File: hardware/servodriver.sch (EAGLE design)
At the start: 17 parts, among them IC1 PIC12F683P, IC2 7805

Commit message: Add the CAM files
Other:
- note added: "2"
- note added: "ServoDriver for the Stockton Marine Science Program. MIT License. (c) 2014 Chris Luke. Source code at https://github.com/chrisy/pic12servo"
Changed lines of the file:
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@@
 <sheet>
 <plain>
+<text x="150.114" y="24.384" size="1.778" layer="91">ServoDriver for the Stockton Marine Science Program.
+MIT License. (c) 2014 Chris Luke.
+Source code at https://github.com/chrisy/pic12servo</text>
+<text x="241.3" y="7.62" size="1.778" layer="91">2</text>
 </plain>
 <instances>
@@
 </schematic>
 </drawing>
+<compatibility>
+<note version="6.3" minversion="6.2.2" severity="warning">
+Since Version 6.2.2 text objects can contain more than one line,
+which will not be processed correctly with this version.
+</note>
+</compatibility>
 </eagle>

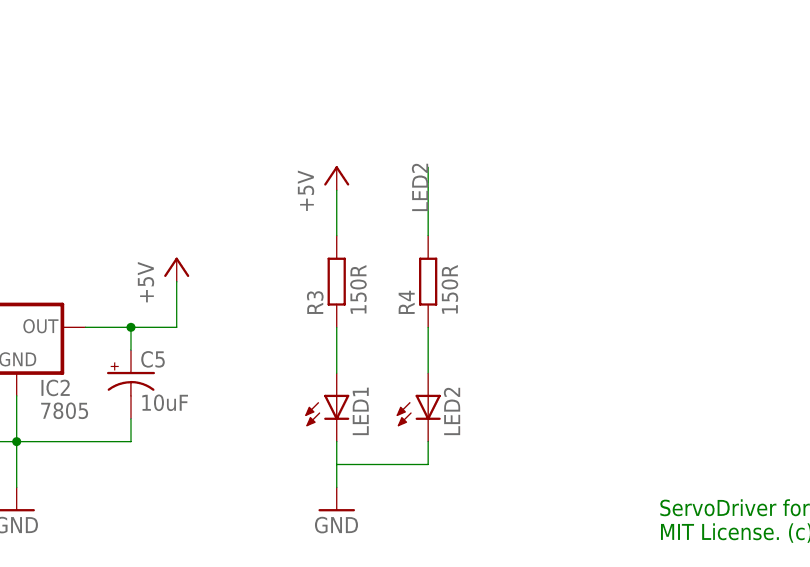
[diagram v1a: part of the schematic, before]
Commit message: Update hardware details, including a BOM
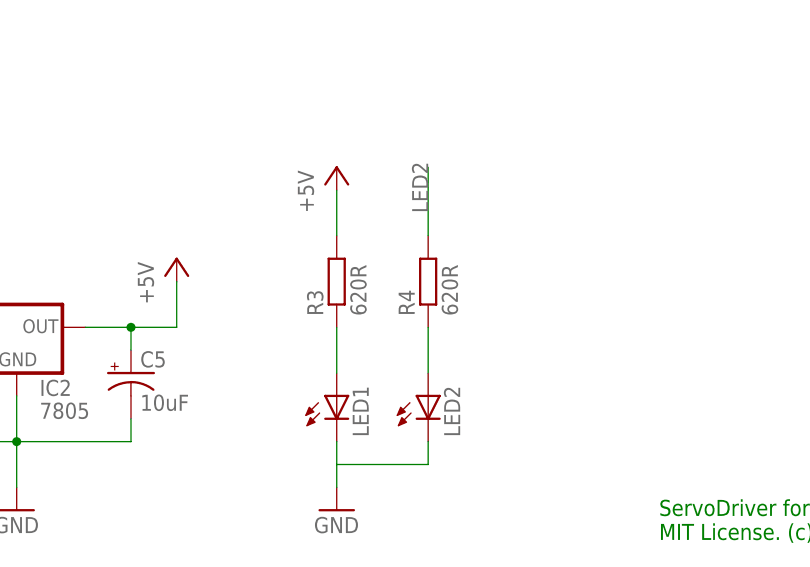
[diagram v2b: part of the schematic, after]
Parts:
- R3, R4: value 150R -> 620R
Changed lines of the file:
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@@
 <part name="R2" library="rcl" deviceset="R-EU_" device="0207/10" value="0R"/>
 <part name="LED1" library="led" deviceset="LED" device="3MM"/>
-<part name="R3" library="rcl" deviceset="R-EU_" device="0207/10" value="150R"/>
+<part name="R3" library="rcl" deviceset="R-EU_" device="0207/10" value="620R"/>
 <part name="P+7" library="supply1" deviceset="+5V" device=""/>
 <part name="GND8" library="supply1" deviceset="GND" device=""/>
 <part name="LED2" library="led" deviceset="LED" device="3MM"/>
-<part name="R4" library="rcl" deviceset="R-EU_" device="0207/10" value="150R"/>
+<part name="R4" library="rcl" deviceset="R-EU_" device="0207/10" value="620R"/>
 </parts>
 <sheets>
